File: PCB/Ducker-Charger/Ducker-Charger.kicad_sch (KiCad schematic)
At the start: 2 parts, among them J1 Conn_01x02, J2 Conn_01x04

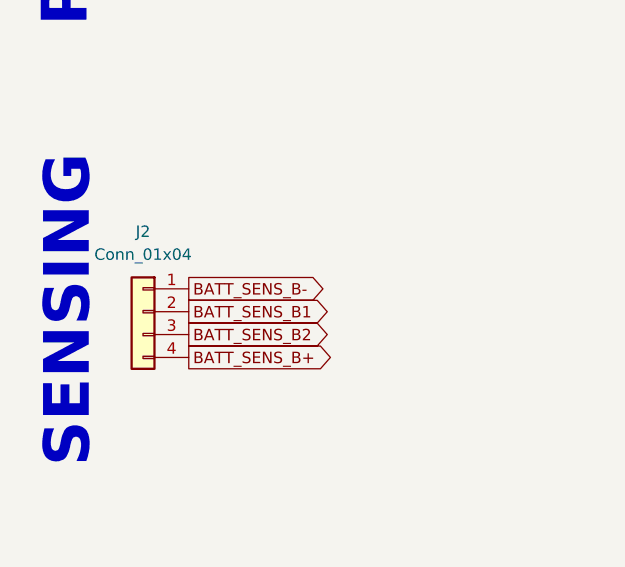
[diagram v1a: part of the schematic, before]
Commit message: fix: changed cell sensing connector
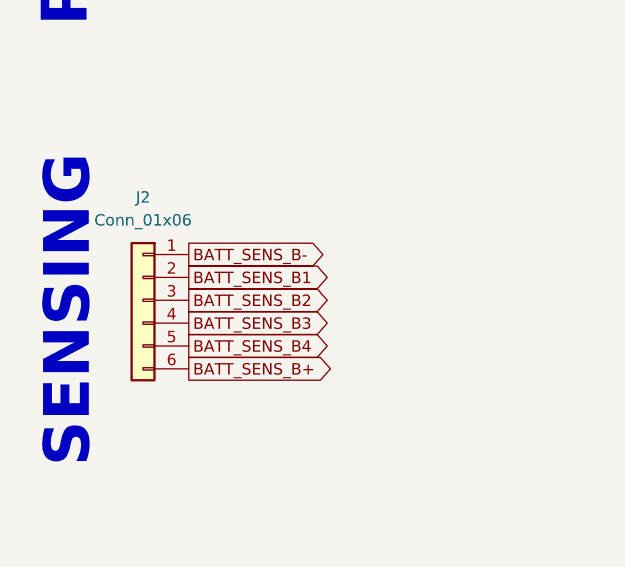
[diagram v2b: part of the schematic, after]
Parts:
- removed J2: Conn_01x04, symbol Connector_Generic:Conn_01x04
- added J2: Conn_01x06, symbol Connector_Generic:Conn_01x06
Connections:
- net BATT_SENS_B+: now also J2.6 (Pin_6)
- net BATT_SENS_B-: now also J2.1 (Pin_1)
- net BATT_SENS_B1: now also J2.2 (Pin_2)
- net BATT_SENS_B2: now also J2.3 (Pin_3)
- new net BATT_SENS_B3: J2.4 (Pin_4)
- new net BATT_SENS_B4: J2.5 (Pin_5)
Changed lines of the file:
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@@
 	(global_label "BATT_SENS_B-"
 		(shape output)
-		(at 35.56 115.57 0)
-		(fields_autoplaced yes)
-		(effects
-			(font
-				(size 1.27 1.27)
-			)
-			(justify left)
-		)
-		(property "Intersheetrefs" "${INTERSHEET_REFS}"
-			(at 52.5151 115.57 0)
+		(at 35.56 111.76 0)
+		(fields_autoplaced yes)
+		(effects
+			(font
+				(size 1.27 1.27)
+			)
+			(justify left)
+		)
+		(property "Intersheetrefs" "${INTERSHEET_REFS}"
+			(at 52.5151 111.76 0)
 			(effects
 				(font
@@
 		)
 	)
+	(global_label "BATT_SENS_B3"
+		(shape output)
+		(at 35.56 119.38 0)
+		(fields_autoplaced yes)
+		(effects
+			(font
+				(size 1.27 1.27)
+			)
+			(justify left)
+		)
+		(property "Intersheetrefs" "${INTERSHEET_REFS}"
+			(at 52.1522 119.38 0)
+			(effects
+				(font
+					(size 1.27 1.27)
+				)
+				(justify left)
+				(hide yes)
+			)
+		)
+	)
+	(global_label "BATT_SENS_B1"
+		(shape output)
+		(at 35.56 114.3 0)
+		(fields_autoplaced yes)
+		(effects
+			(font
+				(size 1.27 1.27)
+			)
+			(justify left)
+		)
+		(property "Intersheetrefs" "${INTERSHEET_REFS}"
+			(at 52.1522 114.3 0)
+			(effects
+				(font
+					(size 1.27 1.27)
+				)
+				(justify left)
+				(hide yes)
+			)
+		)
+	)
 	(global_label "BATT_SENS_B+"
 		(shape output)
-		(at 35.56 123.19 0)
-		(fields_autoplaced yes)
-		(effects
-			(font
-				(size 1.27 1.27)
-			)
-			(justify left)
-		)
-		(property "Intersheetrefs" "${INTERSHEET_REFS}"
-			(at 52.5151 123.19 0)
-			(effects
-				(font
-					(size 1.27 1.27)
-				)
-				(justify left)
-				(hide yes)
-			)
-		)
-	)
-	(global_label "BATT_SENS_B1"
-		(shape output)
-		(at 35.56 118.11 0)
-		(fields_autoplaced yes)
-		(effects
-			(font
-				(size 1.27 1.27)
-			)
-			(justify left)
-		)
-		(property "Intersheetrefs" "${INTERSHEET_REFS}"
-			(at 52.1522 118.11 0)
+		(at 35.56 124.46 0)
+		(fields_autoplaced yes)
+		(effects
+			(font
+				(size 1.27 1.27)
+			)
+			(justify left)
+		)
+		(property "Intersheetrefs" "${INTERSHEET_REFS}"
+			(at 52.5151 124.46 0)
+			(effects
+				(font
+					(size 1.27 1.27)
+				)
+				(justify left)
+				(hide yes)
+			)
+		)
+	)
+	(global_label "BATT_SENS_B4"
+		(shape output)
+		(at 35.56 121.92 0)
+		(fields_autoplaced yes)
+		(effects
+			(font
+				(size 1.27 1.27)
+			)
+			(justify left)
+		)
+		(property "Intersheetrefs" "${INTERSHEET_REFS}"
+			(at 52.1522 121.92 0)
 			(effects
 				(font
@@
 	(global_label "BATT_SENS_B2"
 		(shape output)
-		(at 35.56 120.65 0)
-		(fields_autoplaced yes)
-		(effects
-			(font
-				(size 1.27 1.27)
-			)
-			(justify left)
-		)
-		(property "Intersheetrefs" "${INTERSHEET_REFS}"
-			(at 52.1522 120.65 0)
+		(at 35.56 116.84 0)
+		(fields_autoplaced yes)
+		(effects
+			(font
+				(size 1.27 1.27)
+			)
+			(justify left)
+		)
+		(property "Intersheetrefs" "${INTERSHEET_REFS}"
+			(at 52.1522 116.84 0)
 			(effects
 				(font
@@
 				(justify left)
 				(hide yes)
-			)
-		)
-	)
-	(symbol
-		(lib_id "Connector_Generic:Conn_01x04")
-		(at 30.48 118.11 0)
-		(mirror y)
-		(unit 1)
-		(exclude_from_sim no)
-		(in_bom yes)
-		(on_board yes)
-		(dnp no)
-		(fields_autoplaced yes)
-		(property "Reference" "J2"
-			(at 30.48 109.22 0)
-			(effects
-				(font
-					(size 1.27 1.27)
-				)
-			)
-		)
-		(property "Value" "Conn_01x04"
-			(at 30.48 111.76 0)
-			(effects
-				(font
-					(size 1.27 1.27)
-				)
-			)
-		)
-		(property "Footprint" ""
-			(at 30.48 118.11 0)
-			(effects
-				(font
-					(size 1.27 1.27)
-				)
-				(hide yes)
-			)
-		)
-		(property "Datasheet" "~"
-			(at 30.48 118.11 0)
-			(effects
-				(font
-					(size 1.27 1.27)
-				)
-				(hide yes)
-			)
-		)
-		(property "Description" "Generic connector, single row, 01x04, script generated (kicad-library-utils/schlib/autogen/connector/)"
-			(at 30.48 118.11 0)
-			(effects
-				(font
-					(size 1.27 1.27)
-				)
-				(hide yes)
-			)
-		)
-		(pin "1"
-		)
-		(pin "4"
-		)
-		(pin "3"
-		)
-		(pin "2"
-		)
-		(instances
-			(project ""
-				(path "/74790d6c-a68e-4e6d-b4a9-43de1843f817"
-					(reference "J2")
-					(unit 1)
-				)
 			)
 		)
@@
 					(unit 1)
 				)
+			)
+		)
+	)
+	(symbol
+		(lib_id "Connector_Generic:Conn_01x06")
+		(at 30.48 116.84 0)
+		(mirror y)
+		(unit 1)
+		(exclude_from_sim no)
+		(in_bom yes)
+		(on_board yes)
+		(dnp no)
+		(fields_autoplaced yes)
+		(property "Reference" "J2"
+			(at 30.48 105.41 0)
+			(effects
+				(font
+					(size 1.27 1.27)
+				)
+			)
+		)
+		(property "Value" "Conn_01x06"
+			(at 30.48 107.95 0)
+			(effects
+				(font
+					(size 1.27 1.27)
+				)
+			)
+		)
+		(property "Footprint" ""
+			(at 30.48 116.84 0)
+			(effects
+				(font
+					(size 1.27 1.27)
+				)
+				(hide yes)
+			)
+		)
+		(property "Datasheet" "~"
+			(at 30.48 116.84 0)
+			(effects
+				(font
+					(size 1.27 1.27)
+				)
+				(hide yes)
+			)
+		)
+		(property "Description" "Generic connector, single row, 01x06, script generated (kicad-library-utils/schlib/autogen/connector/)"
+			(at 30.48 116.84 0)
+			(effects
+				(font
+					(size 1.27 1.27)
+				)
+				(hide yes)
+			)
+		)
+		(pin "1"
+		)
+		(pin "4"
+		)
+		(pin "3"
+		)
+		(pin "2"
+		)
+		(pin "6"
+		)
+		(pin "5"
+		)
+		(instances
+			(project ""
+				(path "/74790d6c-a68e-4e6d-b4a9-43de1843f817"
+					(reference "J2")
+					(unit 1)
+				)

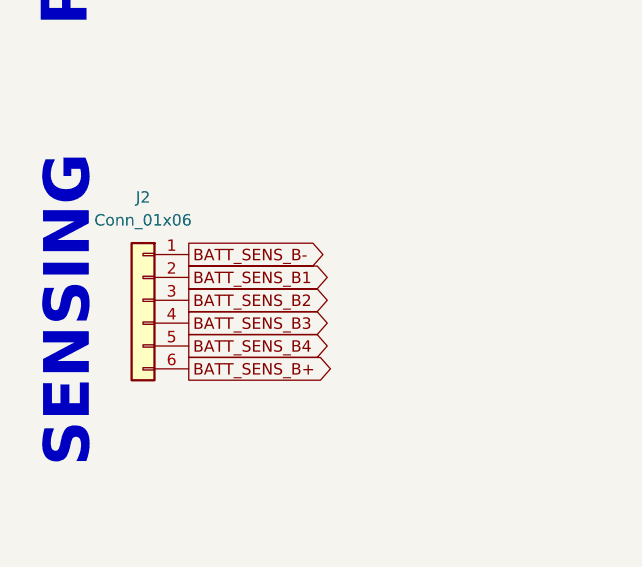
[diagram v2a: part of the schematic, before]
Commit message: feat: started BMS configuration
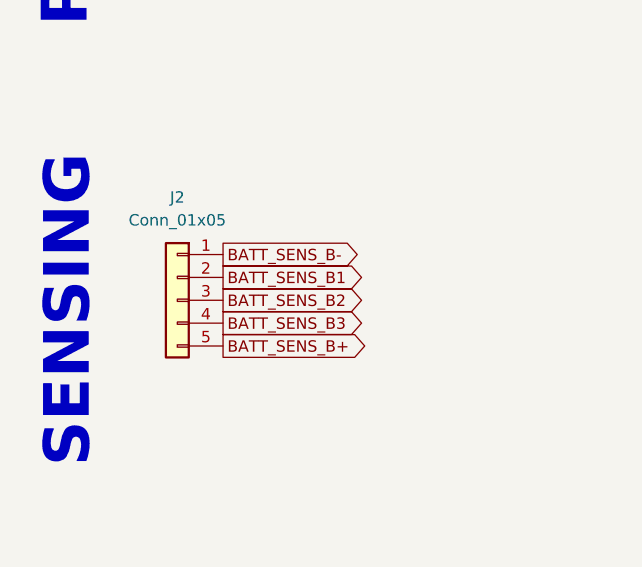
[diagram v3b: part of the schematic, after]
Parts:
- removed J2: Conn_01x06, symbol Connector_Generic:Conn_01x06
- added J2: Conn_01x05, symbol Connector_Generic:Conn_01x05
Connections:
- net BATT_SENS_B+: now also J2.5 (Pin_5)
- net BATT_SENS_B-: now also J2.1 (Pin_1)
- net BATT_SENS_B1: now also J2.2 (Pin_2)
- net BATT_SENS_B2: now also J2.3 (Pin_3)
- net BATT_SENS_B3: now also J2.4 (Pin_4)
